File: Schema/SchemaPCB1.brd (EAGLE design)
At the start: 48.9 x 100 mm, 22 parts, among them J1 CON-HIROSE-COAXIAL-U.FL, J2 Programmer, U1 RN2483, U2 TPS22860DBVR, U3 ESP32, U4 SOT-89-5, U5 SI7217-B-01-IVR

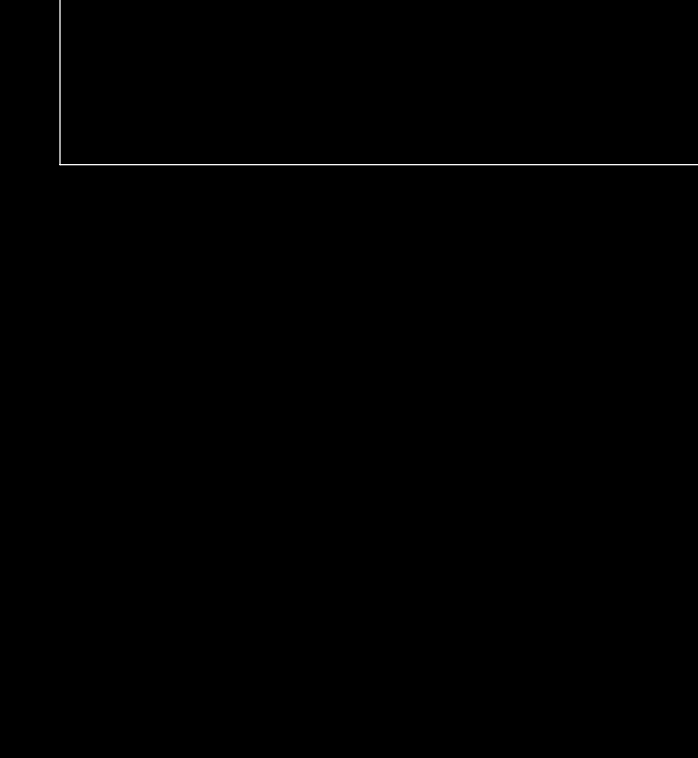
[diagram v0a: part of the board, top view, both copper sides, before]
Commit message: gps toegevoegd
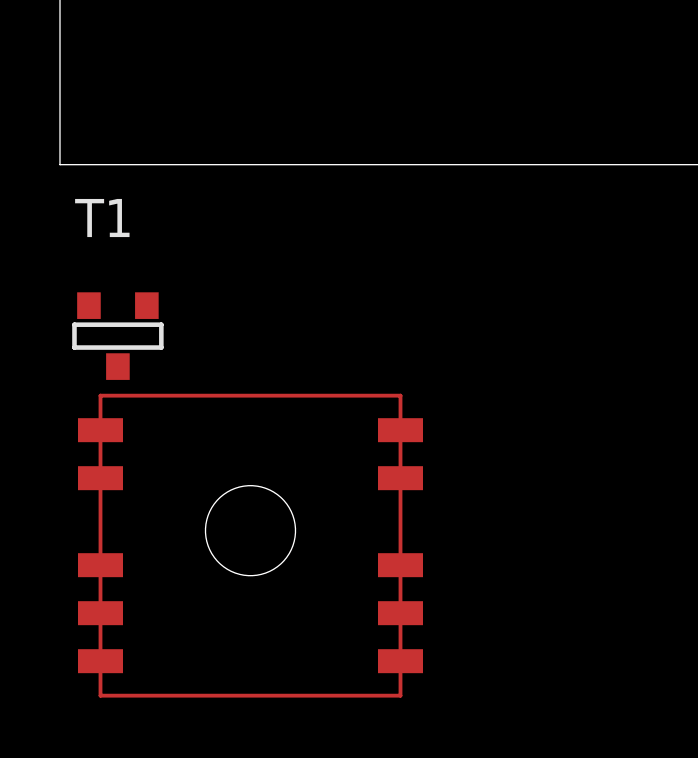
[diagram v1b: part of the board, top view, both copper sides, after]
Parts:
- added T1: (no value), zetex:SOT-23
- added U?1: GPS, gps:GPS
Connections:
- new net *GPS_ENABLE: T1.3, U3.32
- new net N$5: U?1.WAKE-UP
- new net N$6: U?1.NRESET
- new net N$8: T1.2, U?1.VCC
- net +3V3: now also T1.1
- net GND: now also U?1.GND
- net I2C_SCL: now also U?1.I2C_SCL
- net I2C_SDA: now also U?1.I2C_SDA
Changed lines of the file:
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@@
 <attribute name="NAME" x="19.05" y="33.02" size="1.27" layer="25" align="center"/>
 </element>
+<element name="T1" library="zetex" library_urn="urn:adsk.eagle:library:418" package="SOT-23" package3d_urn="urn:adsk.eagle:package:30981/1" value="" x="1.905" y="-5.715" smashed="yes">
+<attribute name="MF" value="" x="1.905" y="-5.715" size="1.778" layer="27" display="off"/>
+<attribute name="MPN" value="" x="1.905" y="-5.715" size="1.778" layer="27" display="off"/>
+<attribute name="NAME" x="0.508" y="-2.413" size="1.27" layer="25" ratio="10"/>
+<attribute name="OC_FARNELL" value="unknown" x="1.905" y="-5.715" size="1.778" layer="27" display="off"/>
+<attribute name="OC_NEWARK" value="unknown" x="1.905" y="-5.715" size="1.778" layer="27" display="off"/>
+<attribute name="POPULARITY" value="15" x="1.905" y="-5.715" size="1.778" layer="27" display="off"/>
+<attribute name="VALUE" x="0.508" y="-3.937" size="1.27" layer="27" ratio="10"/>
+</element>
+<element name="U?1" library="gps" package="GPS" value="GPS" x="6.35" y="-12.7" smashed="yes"/>
 </elements>
 <signals>
@@
 <wire x1="9.525" y1="87.63" x2="9.525" y2="87.31" width="0.6096" layer="1"/>
 <wire x1="1.3208" y1="85.09" x2="1.3208" y2="87.6808" width="0.6096" layer="1"/>
+<contactref element="U?1" pad="GND"/>
 <wire x1="41.275" y1="82.169" x2="41.275" y2="84.76" width="0" layer="19" extent="1-1"/>
 <wire x1="30.48" y1="78.105" x2="30.48" y2="69.215" width="0" layer="19" extent="1-1"/>
@@
 <wire x1="19.07" y1="30.48" x2="29.21" y2="43.815" width="0" layer="19" extent="1-1"/>
 <wire x1="3.175" y1="51.435" x2="12.7" y2="69.215" width="0" layer="19" extent="1-1"/>
+<wire x1="11.35" y1="-14.95" x2="19.07" y2="30.48" width="0" layer="19" extent="1-1"/>
 </signal>
 <signal name="N$1">
@@
 <wire x1="38.3352" y1="57.4548" x2="45.3898" y2="57.4548" width="0.8128" layer="1"/>
 <wire x1="45.3898" y1="57.4548" x2="46.99" y2="59.055" width="0.8128" layer="1"/>
+<contactref element="T1" pad="1"/>
 <wire x1="6.035" y1="50.165" x2="4.46" y2="86.36" width="0" layer="19" extent="1-1"/>
-<wire x1="21.57" y1="29.53" x2="6.035" y2="46.99" width="0" layer="19" extent="1-1"/>
-<wire x1="29.21" y1="45.085" x2="21.57" y2="29.53" width="0" layer="19" extent="1-1"/>
+<wire x1="29.21" y1="45.085" x2="6.035" y2="46.99" width="0" layer="19" extent="1-1"/>
+<wire x1="21.57" y1="29.53" x2="29.21" y2="45.085" width="0" layer="19" extent="1-1"/>
+<wire x1="1.9304" y1="-6.731" x2="21.57" y2="29.53" width="0" layer="19" extent="1-1"/>
 </signal>
 <signal name="ESP32_EN">
@@
 <wire x1="1.4224" y1="52.2224" x2="1.4224" y2="46.2026" width="0.8128" layer="1"/>
 <wire x1="6.985" y1="45.085" x2="7.935" y2="46.035" width="0.8128" layer="1"/>
+<contactref element="U?1" pad="I2C_SCL"/>
+<wire x1="1.35" y1="-10.45" x2="7.935" y2="46.99" width="0" layer="19" extent="1-1"/>
 </signal>
 <signal name="I2C_SDA">
@@
 <wire x1="6.985" y1="52.07" x2="8.255" y2="50.8" width="0.8128" layer="1"/>
 <wire x1="8.255" y1="50.8" x2="8.255" y2="50.165" width="0.8128" layer="1"/>
+<contactref element="U?1" pad="I2C_SDA"/>
+<wire x1="1.35" y1="-8.85" x2="7.935" y2="50.165" width="0" layer="19" extent="1-1"/>
 </signal>
 <signal name="HALL_DATA">
@@
 <wire x1="38.1" y1="79.06" x2="38.42" y2="78.74" width="0.8128" layer="1"/>
 </signal>
+<signal name="*GPS_ENABLE">
+<contactref element="T1" pad="3"/>
+<contactref element="U3" pad="32"/>
+<wire x1="2.8956" y1="-4.699" x2="12.21" y2="51.435" width="0" layer="19" extent="1-1"/>
+</signal>
+<signal name="N$8">
+<contactref element="T1" pad="2"/>
+<contactref element="U?1" pad="VCC"/>
+<wire x1="11.35" y1="-8.85" x2="0.9652" y2="-4.699" width="0" layer="19" extent="1-1"/>
+</signal>
+<signal name="N$6">
+<contactref element="U?1" pad="NRESET"/>
+</signal>
+<signal name="N$5">
+<contactref element="U?1" pad="WAKE-UP"/>
+</signal>
 </signals>
 <mfgpreviewcolors>
@@
 </drawing>
 <compatibility>
+<note version="8.2" severity="warning">
+Since Version 8.2, EAGLE supports online libraries. The ids
+of those online libraries will not be understood (or retained)
+with this version.
+</note>
 <note version="8.3" severity="warning">
 Since Version 8.3, EAGLE supports URNs for individual library
